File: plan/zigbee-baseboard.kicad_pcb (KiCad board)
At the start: 4 copper layers, 11.5 x 17.8 mm, 55 parts, among them J1 Debug_SWD_Pogo_2x3, J2 EFR32MG24_Core_Expansion_2x6, SW1 EVPBB2A9B000, U1 EFR32MG24B020F1536IM48-B, Y1 XTL501250-S315-038

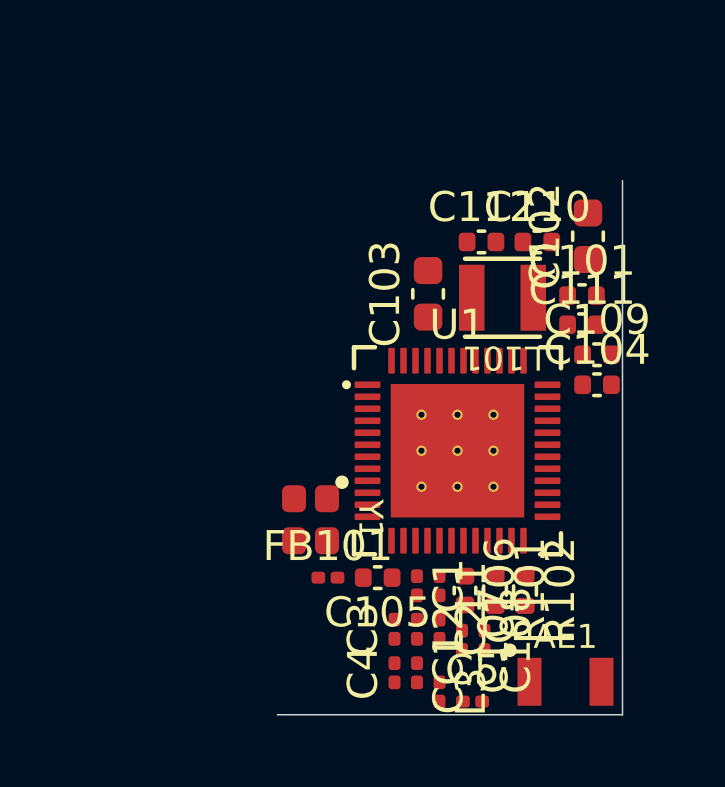
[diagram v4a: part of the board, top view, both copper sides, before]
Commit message: Place keepout-zone for antenna area
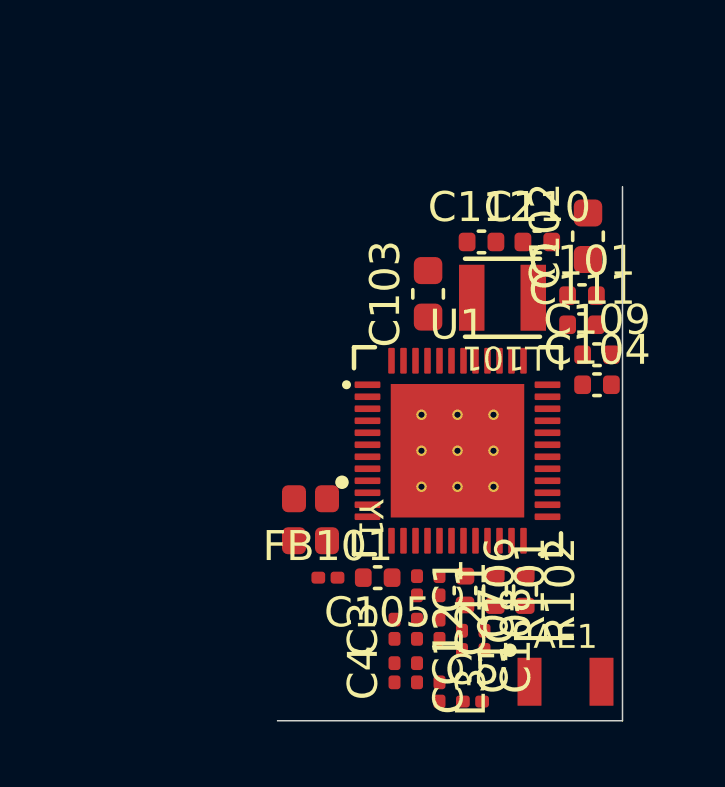
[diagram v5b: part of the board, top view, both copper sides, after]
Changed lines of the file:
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@@
 		(embedded_fonts no)
 	)
-	(gr_rect
-		(start 142 98.3)
-		(end 148.5 102.3)
-		(stroke
-			(width 0.1)
-			(type default)
-		)
-		(fill no)
-		(layer "Dwgs.User")
-	)
 	(gr_line
-		(start 137 102.3)
-		(end 148.5 102.3)
+		(start 137 102.5)
+		(end 148.5 102.5)
 		(stroke
 			(width 0.05)
@@
 	)
 	(gr_line
-		(start 148.5 84.5)
-		(end 148.5 102.3)
+		(start 148.5 84.7)
+		(end 148.5 102.5)
 		(stroke
 			(width 0.05)
@@
 		(layer "Edge.Cuts")
 	)
+	(zone
+		(layers "F.Cu" "B.Cu" "In1.Cu" "In2.Cu")
+		(name "Keepout-Antenna")
+		(hatch edge 0.5)
+		(connect_pads
+			(clearance 0)
+		)
+		(min_thickness 0.25)
+		(keepout
+			(tracks not_allowed)
+			(vias not_allowed)
+			(pads allowed)
+			(copperpour not_allowed)
+			(footprints allowed)
+		)
+		(placement
+			(enabled no)
+			(sheetname "/Expansion/")
+		)
+		(fill
+			(thermal_gap 0.5)
+			(thermal_bridge_width 0.5)
+			(island_removal_mode 0)
+		)
+		(polygon
+			(pts
+				(xy 142 98.5) (xy 148.5 98.5) (xy 148.5 102.5) (xy 142 102.5)
+			)
+		)
+	)
 	(embedded_fonts no)

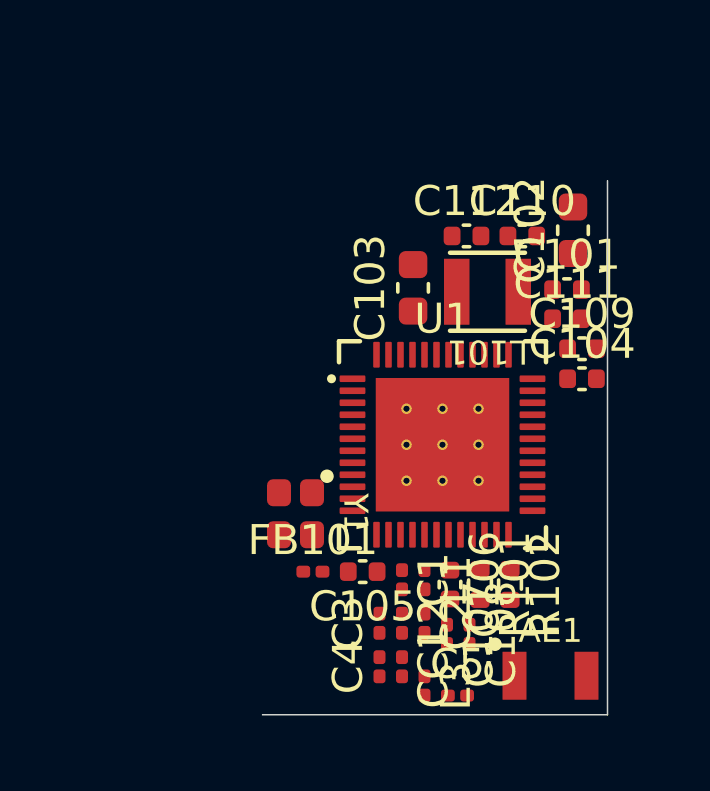
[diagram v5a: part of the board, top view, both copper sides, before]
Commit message: Adapt antenna keepout area and device placement
- Increase board size at the lower right edge for better placement
- Avoid GND pads inside of keepout area
- Move C2 and C106 out of antenna area
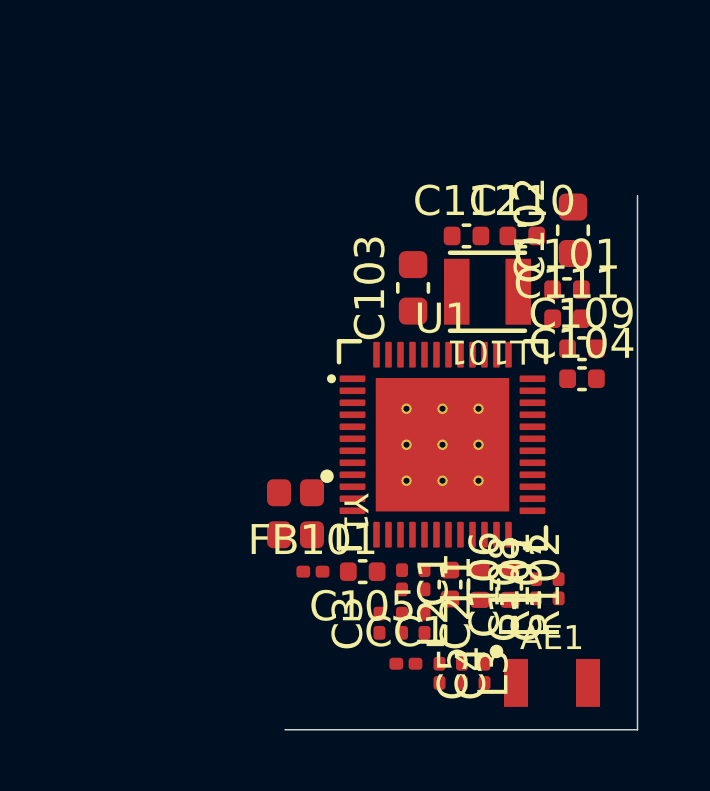
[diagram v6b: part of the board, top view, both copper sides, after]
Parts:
- moved C107 4.02 mm to (146.9, 98.3), turned to 90 degrees
- moved C108 2.69 mm to (146.1, 98.3), turned to 90 degrees
- moved C4 2.01 mm to (142.9, 101.1), turned to -90 degrees
- moved L3 1.32 mm to (143.7, 101.1)
- moved C5 1.17 mm to (144.4, 101.1), turned to 90 degrees
- moved AE1 0.25 mm to (146.7, 101.4)
- moved CC1 0.16 mm to (141.8, 100.8), turned to 0 degrees
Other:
- board size 11.5 x 17.8 mm -> 11.8 x 17.8 mm
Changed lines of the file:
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@@
 	)
 	(footprint "Capacitor_SMD:C_0201_0603Metric"
-		(locked yes)
 		(layer "F.Cu")
-		(at 140.9 100.9 90)
+		(at 142.9 101.12 -90)
 		(descr "Capacitor SMD 0201 (0603 Metric), square (rectangular) end terminal, IPC-7351 nominal, (Body size source: https://www.vishay.com/docs/20052/crcw0201e3.pdf)")
 		(tags "capacitor")
@@
 		)
 		(pad "" smd roundrect
-			(at -0.345 0 90)
+			(at -0.345 0 270)
 			(size 0.318 0.36)
 			(layers "F.Paste")
@@
 		)
 		(pad "" smd roundrect
-			(at 0.345 0 90)
+			(at 0.345 0 270)
 			(size 0.318 0.36)
 			(layers "F.Paste")
@@
 		)
 		(pad "1" smd roundrect
-			(at -0.32 0 90)
+			(at -0.32 0 270)
 			(size 0.46 0.4)
 			(layers "F.Cu" "F.Mask")
@@
 		)
 		(pad "2" smd roundrect
-			(at 0.32 0 90)
+			(at 0.32 0 270)
 			(size 0.46 0.4)
 			(layers "F.Cu" "F.Mask")
@@
 	)
 	(footprint "Capacitor_SMD:C_0201_0603Metric"
-		(locked yes)
 		(layer "F.Cu")
-		(at 143.5 101.86)
+		(at 144.4 101.12 90)
 		(descr "Capacitor SMD 0201 (0603 Metric), square (rectangular) end terminal, IPC-7351 nominal, (Body size source: https://www.vishay.com/docs/20052/crcw0201e3.pdf)")
 		(tags "capacitor")
 		(property "Reference" "C5"
-			(at 0 -1.05 0)
+			(at 0 -1.05 90)
 			(layer "F.SilkS")
 			(effects
@@
 		)
 		(property "Value" "TUNE"
-			(at 0 1.05 0)
+			(at 0 1.05 90)
 			(layer "F.Fab")
 			(effects
@@
 		)
 		(property "Datasheet" ""
-			(at 0 0 0)
+			(at 0 0 90)
 			(layer "F.Fab")
 			(hide yes)
@@
 		)
 		(property "Description" "0201"
-			(at 0 0 0)
+			(at 0 0 90)
 			(layer "F.Fab")
 			(hide yes)
@@
 		)
 		(property "KiLib_Generator" "SMD_2terminal_chip_molded"
-			(at 0 0 0)
+			(at 0 0 90)
 			(layer "F.SilkS")
 			(hide yes)
@@
 		)
 		(fp_text user "${REFERENCE}"
-			(at 0 -0.68 0)
+			(at 0 -0.68 90)
 			(layer "F.Fab")
 			(effects
@@
 		)
 		(pad "" smd roundrect
-			(at -0.345 0)
+			(at -0.345 0 90)
 			(size 0.318 0.36)
 			(layers "F.Paste")
@@
 		)
 		(pad "" smd roundrect
-			(at 0.345 0)
+			(at 0.345 0 90)
 			(size 0.318 0.36)
 			(layers "F.Paste")
@@
 		)
 		(pad "1" smd roundrect
-			(at -0.32 0)
+			(at -0.32 0 90)
 			(size 0.46 0.4)
 			(layers "F.Cu" "F.Mask")
@@
 		)
 		(pad "2" smd roundrect
-			(at 0.32 0)
+			(at 0.32 0 90)
 			(size 0.46 0.4)
 			(layers "F.Cu" "F.Mask")
@@
 	)
 	(footprint "Capacitor_SMD:C_0201_0603Metric"
-		(locked yes)
 		(layer "F.Cu")
-		(at 143.9 99.82 -90)
+		(at 146.12 98.3 90)
 		(descr "Capacitor SMD 0201 (0603 Metric), square (rectangular) end terminal, IPC-7351 nominal, (Body size source: https://www.vishay.com/docs/20052/crcw0201e3.pdf)")
 		(tags "capacitor")
@@
 		)
 		(pad "" smd roundrect
-			(at -0.345 0 270)
+			(at -0.345 0 90)
 			(size 0.318 0.36)
 			(layers "F.Paste")
@@
 		)
 		(pad "" smd roundrect
-			(at 0.345 0 270)
+			(at 0.345 0 90)
 			(size 0.318 0.36)
 			(layers "F.Paste")
@@
 		)
 		(pad "1" smd roundrect
-			(at -0.32 0 270)
+			(at -0.32 0 90)
 			(size 0.46 0.4)
 			(layers "F.Cu" "F.Mask")
@@
 		)
 		(pad "2" smd roundrect
-			(at 0.32 0 270)
+			(at 0.32 0 90)
 			(size 0.46 0.4)
 			(layers "F.Cu" "F.Mask")
@@
 	(footprint "Inductor_SMD:L_0201_0603Metric"
 		(layer "F.Cu")
-		(at 142.4 101.54 -90)
+		(at 143.65 101.12 -90)
 		(descr "Inductor SMD 0201 (0603 Metric), square (rectangular) end terminal, IPC-7351 nominal, (Body size source: https://www.vishay.com/docs/20052/crcw0201e3.pdf)")
 		(tags "inductor")
@@
 	(footprint "Capacitor_SMD:C_0201_0603Metric"
 		(layer "F.Cu")
-		(at 143.15 99.82 -90)
+		(at 146.87 98.3 90)
 		(descr "Capacitor SMD 0201 (0603 Metric), square (rectangular) end terminal, IPC-7351 nominal, (Body size source: https://www.vishay.com/docs/20052/crcw0201e3.pdf)")
 		(tags "capacitor")
@@
 		)
 		(pad "" smd roundrect
-			(at -0.345 0 270)
+			(at -0.345 0 90)
 			(size 0.318 0.36)
 			(layers "F.Paste")
@@
 		)
 		(pad "" smd roundrect
-			(at 0.345 0 270)
+			(at 0.345 0 90)
 			(size 0.318 0.36)
 			(layers "F.Paste")
@@
 		)
 		(pad "1" smd roundrect
-			(at -0.32 0 270)
+			(at -0.32 0 90)
 			(size 0.46 0.4)
 			(layers "F.Cu" "F.Mask")
@@
 		)
 		(pad "2" smd roundrect
-			(at 0.32 0 270)
+			(at 0.32 0 90)
 			(size 0.46 0.4)
 			(layers "F.Cu" "F.Mask")
@@
 	)
 	(footprint "Resistor_SMD:R_0201_0603Metric"
-		(locked yes)
 		(layer "F.Cu")
-		(at 141.65 100.9 -90)
+		(at 141.78 100.8)
 		(descr "Resistor SMD 0201 (0603 Metric), square (rectangular) end terminal, IPC-7351 nominal, (Body size source: https://www.vishay.com/docs/20052/crcw0201e3.pdf)")
 		(tags "resistor")
 		(property "Reference" "CC1"
-			(at 0 -1.05 90)
+			(at 0 -1.05 0)
 			(layer "F.SilkS")
 			(effects
@@
 		)
 		(property "Value" "0 Ω"
-			(at 0 1.05 90)
+			(at 0 1.05 0)
 			(layer "F.Fab")
 			(effects
@@
 		)
 		(property "Datasheet" ""
-			(at 0 0 90)
+			(at 0 0 0)
 			(layer "F.Fab")
 			(hide yes)
@@
 		)
 		(property "Description" "0201"
-			(at 0 0 90)
+			(at 0 0 0)
 			(layer "F.Fab")
 			(hide yes)
@@
 		)
 		(property "KiLib_Generator" "SMD_2terminal_chip_molded"
-			(at 0 0 90)
+			(at 0 0 0)
 			(layer "F.SilkS")
 			(hide yes)
@@
 		)
 		(fp_text user "${REFERENCE}"
-			(at 0 -0.68 90)
+			(at 0 -0.68 0)
 			(layer "F.Fab")
 			(effects
@@
 		)
 		(pad "" smd roundrect
-			(at -0.345 0 270)
+			(at -0.345 0)
 			(size 0.318 0.36)
 			(layers "F.Paste")
@@
 		)
 		(pad "" smd roundrect
-			(at 0.345 0 270)
+			(at 0.345 0)
 			(size 0.318 0.36)
 			(layers "F.Paste")
@@
 		)
 		(pad "1" smd roundrect
-			(at -0.32 0 270)
+			(at -0.32 0)
 			(size 0.46 0.4)
 			(layers "F.Cu" "F.Mask")
@@
 		)
 		(pad "2" smd roundrect
-			(at 0.32 0 270)
+			(at 0.32 0)
 			(size 0.46 0.4)
 			(layers "F.Cu" "F.Mask")
@@
 	(footprint "Smarthome:Antenna_Johanson_2450AT18A0100001E"
 		(layer "F.Cu")
-		(at 146.6 101.2)
+		(at 146.65 101.44)
 		(property "Reference" "AE1"
 			(at 0 -1.5 0)
@@
 	)
 	(footprint "Capacitor_SMD:C_0201_0603Metric"
-		(locked yes)
 		(layer "F.Cu")
 		(at 142.4 99.45 -90)
@@
 	)
 	(gr_line
-		(start 137 102.5)
-		(end 148.5 102.5)
+		(start 137.75 103)
+		(end 149.5 103)
 		(stroke
 			(width 0.05)
@@
 	)
 	(gr_line
-		(start 148.5 84.7)
-		(end 148.5 102.5)
+		(start 149.5 85.2)
+		(end 149.5 103)
 		(stroke
 			(width 0.05)
@@
 		(min_thickness 0.25)
 		(keepout
-			(tracks not_allowed)
+			(tracks allowed)
 			(vias not_allowed)
 			(pads allowed)
@@
 		(polygon
 			(pts
-				(xy 142 98.5) (xy 148.5 98.5) (xy 148.5 102.5) (xy 142 102.5)
+				(xy 143 99) (xy 149.5 99) (xy 149.5 103) (xy 143 103)
 			)
 		)

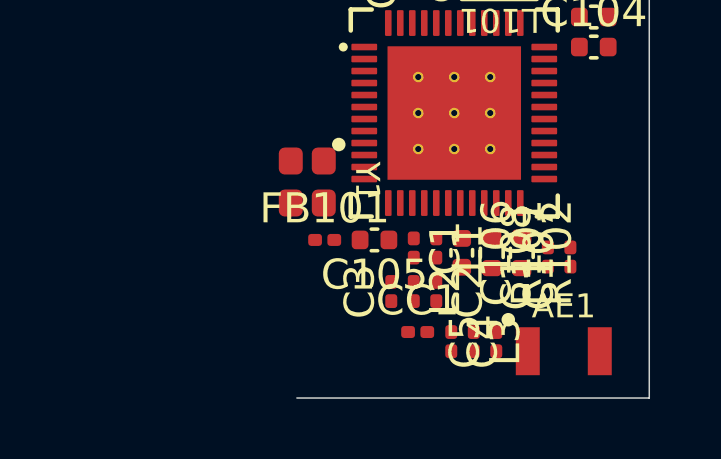
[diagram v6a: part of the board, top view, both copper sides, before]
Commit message: Place GND vias for antenna tuning
- place small GND vias next to GND pads of antenna tuning devices (C4, C5)
- adapt position so that GND vias can get placed perfectly with minimum track length
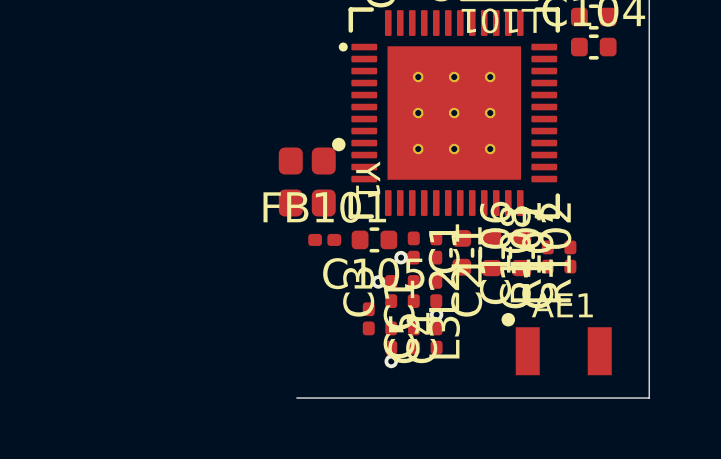
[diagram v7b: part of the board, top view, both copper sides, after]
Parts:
- moved C4 2.00 mm to (140.9, 101.0)
- moved C5 1.99 mm to (142.4, 101.0)
- moved L3 1.99 mm to (141.7, 101.0)
- moved CC1 1.69 mm to (140.2, 100.4), turned to -90 degrees
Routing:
- net GND: track 0.00 -> 2.24 mm, vias 0 -> 4
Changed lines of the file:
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@@
 	(footprint "Capacitor_SMD:C_0201_0603Metric"
 		(layer "F.Cu")
-		(at 142.9 101.12 -90)
+		(at 140.9 101 -90)
 		(descr "Capacitor SMD 0201 (0603 Metric), square (rectangular) end terminal, IPC-7351 nominal, (Body size source: https://www.vishay.com/docs/20052/crcw0201e3.pdf)")
 		(tags "capacitor")
@@
 	(footprint "Capacitor_SMD:C_0201_0603Metric"
 		(layer "F.Cu")
-		(at 144.4 101.12 90)
+		(at 142.41 101 90)
 		(descr "Capacitor SMD 0201 (0603 Metric), square (rectangular) end terminal, IPC-7351 nominal, (Body size source: https://www.vishay.com/docs/20052/crcw0201e3.pdf)")
 		(tags "capacitor")
@@
 	)
 	(footprint "Capacitor_SMD:C_0201_0603Metric"
-		(locked yes)
 		(layer "F.Cu")
 		(at 141.65 98 -90)
@@
 	(footprint "Inductor_SMD:L_0201_0603Metric"
 		(layer "F.Cu")
-		(at 143.65 101.12 -90)
+		(at 141.66 101 -90)
 		(descr "Inductor SMD 0201 (0603 Metric), square (rectangular) end terminal, IPC-7351 nominal, (Body size source: https://www.vishay.com/docs/20052/crcw0201e3.pdf)")
 		(tags "inductor")
@@
 	)
 	(footprint "Capacitor_SMD:C_0201_0603Metric"
-		(locked yes)
 		(layer "F.Cu")
 		(at 140.9 99.45 90)
@@
 	(footprint "Resistor_SMD:R_0201_0603Metric"
 		(layer "F.Cu")
-		(at 141.78 100.8)
+		(at 140.15 100.36 -90)
 		(descr "Resistor SMD 0201 (0603 Metric), square (rectangular) end terminal, IPC-7351 nominal, (Body size source: https://www.vishay.com/docs/20052/crcw0201e3.pdf)")
 		(tags "resistor")
 		(property "Reference" "CC1"
-			(at 0 -1.05 0)
+			(at 0 -1.05 90)
 			(layer "F.SilkS")
 			(effects
@@
 		)
 		(property "Value" "0 Ω"
-			(at 0 1.05 0)
+			(at 0 1.05 90)
 			(layer "F.Fab")
 			(effects
@@
 		)
 		(property "Datasheet" ""
-			(at 0 0 0)
+			(at 0 0 90)
 			(layer "F.Fab")
 			(hide yes)
@@
 		)
 		(property "Description" "0201"
-			(at 0 0 0)
+			(at 0 0 90)
 			(layer "F.Fab")
 			(hide yes)
@@
 		)
 		(property "KiLib_Generator" "SMD_2terminal_chip_molded"
-			(at 0 0 0)
+			(at 0 0 90)
 			(layer "F.SilkS")
 			(hide yes)
@@
 		)
 		(fp_text user "${REFERENCE}"
-			(at 0 -0.68 0)
+			(at 0 -0.68 90)
 			(layer "F.Fab")
 			(effects
@@
 		)
 		(pad "" smd roundrect
-			(at -0.345 0)
+			(at -0.345 0 270)
 			(size 0.318 0.36)
 			(layers "F.Paste")
@@
 		)
 		(pad "" smd roundrect
-			(at 0.345 0)
+			(at 0.345 0 270)
 			(size 0.318 0.36)
 			(layers "F.Paste")
@@
 		)
 		(pad "1" smd roundrect
-			(at -0.32 0)
+			(at -0.32 0 270)
 			(size 0.46 0.4)
 			(layers "F.Cu" "F.Mask")
@@
 		)
 		(pad "2" smd roundrect
-			(at 0.32 0)
+			(at 0.32 0 270)
 			(size 0.46 0.4)
 			(layers "F.Cu" "F.Mask")
@@
 		(layer "Edge.Cuts")
 	)
+	(segment
+		(start 142.451143 100.221802)
+		(end 142.4 100.170659)
+		(width 0.2)
+		(layer "F.Cu")
+		(net "GND")
+	)
+	(segment
+		(start 141.65 98.32)
+		(end 141.226206 98.32)
+		(width 0.3)
+		(layer "F.Cu")
+		(net "GND")
+	)
+	(segment
+		(start 140.9 99.13)
+		(end 140.47 99.13)
+		(width 0.3)
+		(layer "F.Cu")
+		(net "GND")
+	)
+	(segment
+		(start 142.4 100.170659)
+		(end 142.4 99.77)
+		(width 0.3)
+		(layer "F.Cu")
+		(net "GND")
+	)
+	(segment
+		(start 140.9 101.32)
+		(end 140.9 101.78)
+		(width 0.3)
+		(layer "F.Cu")
+		(net "GND")
+	)
+	(segment
+		(start 142.41 100.68)
+		(end 142.41 100.221802)
+		(width 0.3)
+		(layer "F.Cu")
+		(net "GND")
+	)
+	(via
+		(at 141.226206 98.32)
+		(size 0.45)
+		(drill 0.2)
+		(layers "F.Cu" "B.Cu")
+		(net "GND")
+	)
+	(via
+		(at 142.41 100.221802)
+		(size 0.45)
+		(drill 0.2)
+		(layers "F.Cu" "B.Cu")
+		(net "GND")
+	)
+	(via
+		(at 140.9 101.78)
+		(size 0.45)
+		(drill 0.2)
+		(layers "F.Cu" "B.Cu")
+		(net "GND")
+	)
+	(via
+		(at 140.47 99.13)
+		(size 0.45)
+		(drill 0.2)
+		(layers "F.Cu" "B.Cu")
+		(net "GND")
+	)
 	(zone

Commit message: Route MG24 Matching network
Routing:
- net RF2G4_IO: track 0.00 -> 2.07 mm
- net Net-(C3-Pad1): track 0.00 -> 1.61 mm
- net Net-(C2-Pad1): track 0.00 -> 1.56 mm
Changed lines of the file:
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@@
 		(net "GND")
+	)
+	(segment
+		(start 142 97.33)
+		(end 141.65 97.68)
+		(width 0.2631)
+		(layer "F.Cu")
+		(net "RF2G4_IO")
+	)
+	(segment
+		(start 142 96.5)
+		(end 142 97.33)
+		(width 0.2631)
+		(layer "F.Cu")
+		(net "RF2G4_IO")
+	)
+	(segment
+		(start 141.65 97.68)
+		(end 142.4 97.68)
+		(width 0.2631)
+		(layer "F.Cu")
+		(net "RF2G4_IO")
+	)
+	(segment
+		(start 140.9 99.77)
+		(end 140.42 99.77)
+		(width 0.2)
+		(layer "F.Cu")
+		(net "Net-(C3-Pad1)")
+	)
+	(segment
+		(start 140.42 99.77)
+		(end 140.15 100.04)
+		(width 0.2)
+		(layer "F.Cu")
+		(net "Net-(C3-Pad1)")
+	)
+	(segment
+		(start 141.65 99.77)
+		(end 140.9 99.77)
+		(width 0.2)
+		(layer "F.Cu")
+		(net "Net-(C3-Pad1)")
+	)
+	(segment
+		(start 142.4 98.32)
+		(end 142.4 99.13)
+		(width 0.2)
+		(layer "F.Cu")
+		(net "Net-(C2-Pad1)")
+	)
+	(segment
+		(start 142.4 99.13)
+		(end 141.65 99.13)
+		(width 0.2)
+		(layer "F.Cu")
+		(net "Net-(C2-Pad1)")
 	)
 	(zone
